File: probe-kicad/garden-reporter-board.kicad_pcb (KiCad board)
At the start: 2 copper layers, 21 parts, among them J1 70543-0106, J2 Conn_01x02, J3 70543-0002, J4 70543-0002, J5 70543-0002, Q1 TN0702N3-G, U1 MCP1700-3302E_TO92, U2 MCP1700-3302E_TO92

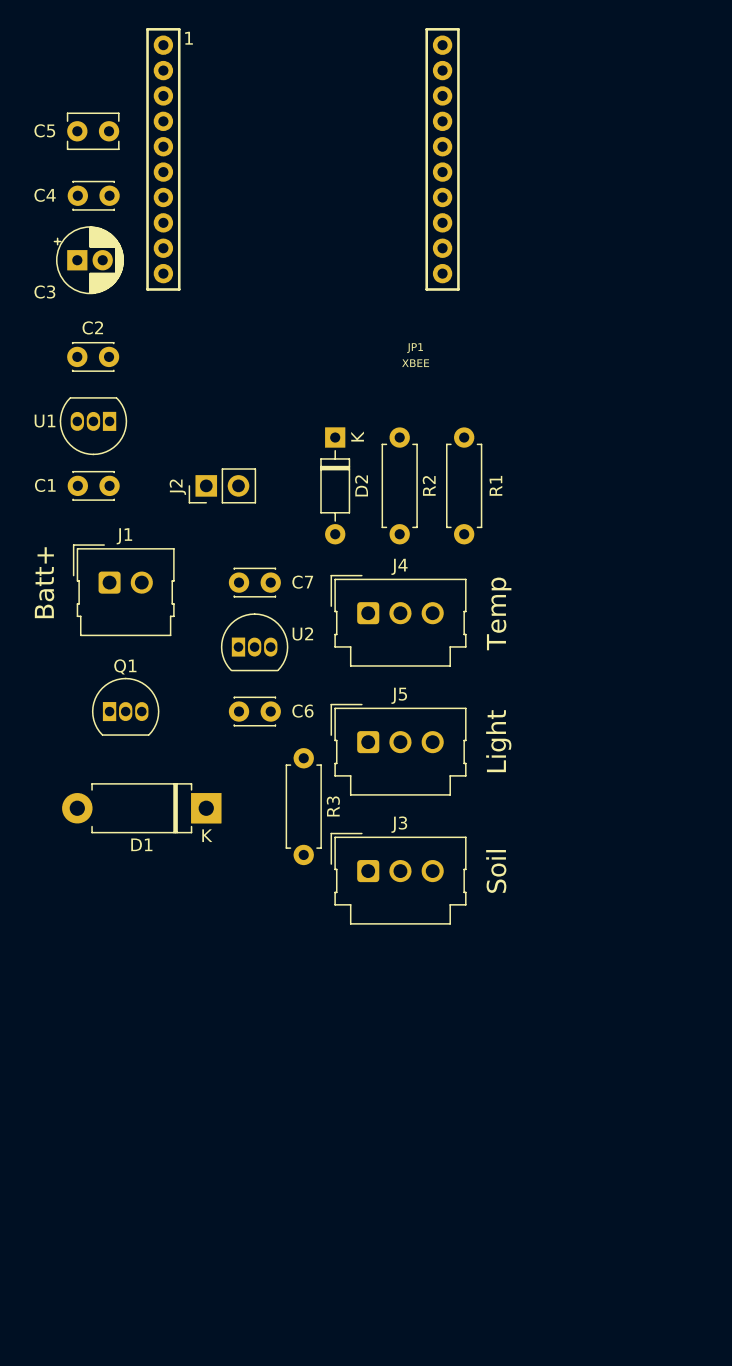
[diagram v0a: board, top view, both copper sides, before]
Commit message: Feature/probe pcb edge and routing
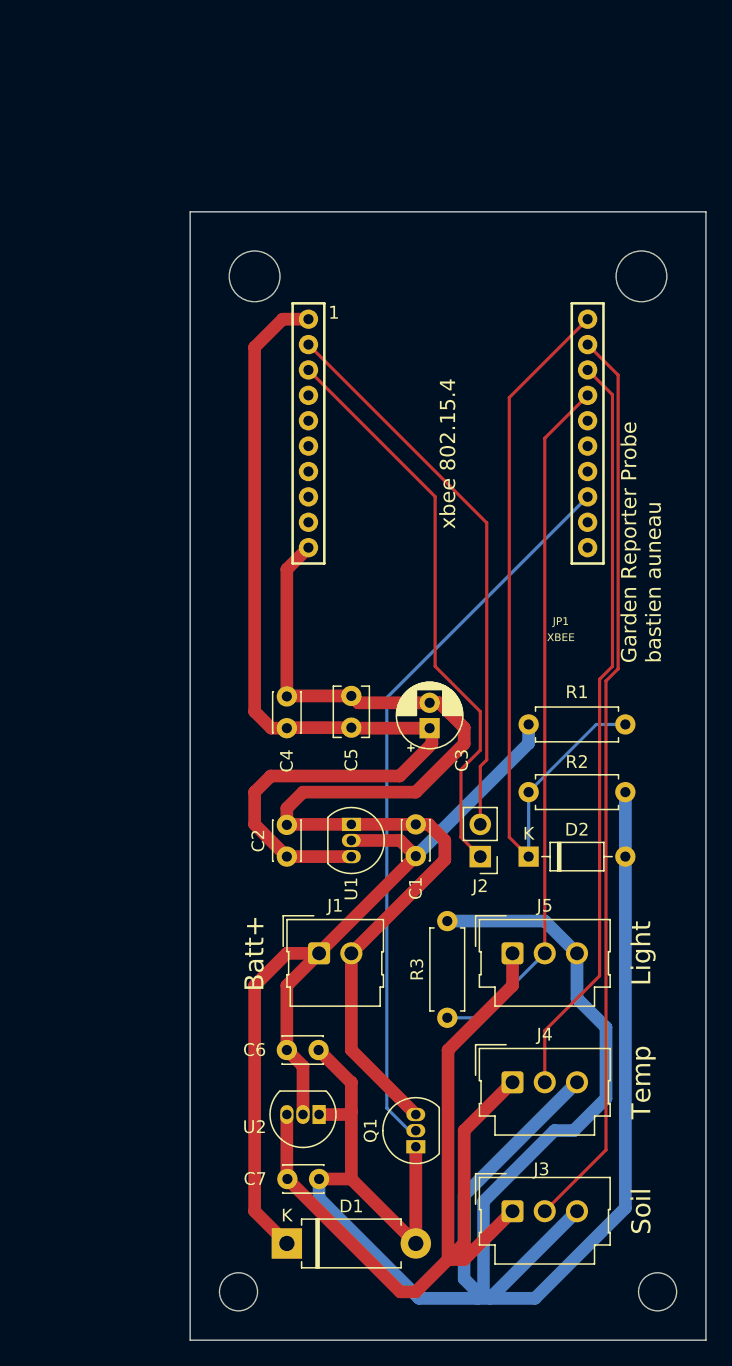
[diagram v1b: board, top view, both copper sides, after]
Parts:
- moved C5 51.7 mm to (146.1, 95.2), turned to 90 degrees
- moved C7 47.0 mm to (141.0, 130.8), turned to 0 degrees
- moved C3 46.2 mm to (152.2, 95.3), turned to 90 degrees
- moved C4 45.1 mm to (141.0, 95.3), turned to 90 degrees
- moved C2 42.7 mm to (141.0, 105.4), turned to 90 degrees
- moved Q1 41.9 mm to (151.1, 128.3), turned to 90 degrees
- moved C1 39.5 mm to (151.1, 105.4), turned to 90 degrees
- moved J4 38.7 mm to (158.8, 123.2)
- moved U2 37.4 mm to (143.5, 125.7), turned to 180 degrees
- moved U1 37.0 mm to (146.1, 102.9), turned to -90 degrees
- moved D2 36.4 mm to (160.0, 105.4), turned to 0 degrees
- moved J2 36.3 mm to (156.2, 105.4), turned to 180 degrees
- moved D1 34.9 mm to (141.0, 135.9), turned to 0 degrees
- moved J1 33.6 mm to (143.5, 113.0)
- moved R2 29.7 mm to (160.0, 100.3), turned to 0 degrees
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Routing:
- net GND1: track 0.00 -> 171.2 mm
- net -BATT: track 0.00 -> 85.8 mm
- net +3.3V: track 0.00 -> 76.3 mm
- net +BATT: track 0.00 -> 72.2 mm
- net /sensor_soil: track 0.00 -> 71.7 mm
- net +3.3VADC: track 0.00 -> 71.5 mm
- net /sensor_batt: track 0.00 -> 60.4 mm
- net /sensor_temp: track 0.00 -> 59.1 mm
- net /xbee_ON: track 0.00 -> 57.7 mm
- net /sensor_light: track 0.00 -> 55.1 mm
- net Net-(J2-Pad1): track 0.00 -> 45.2 mm
- net Net-(J2-Pad2): track 0.00 -> 43.8 mm
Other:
- board outline added: 40.6 x 88.9 mm
- board text added: "Garden Reporter Probe bastien auneau"
- board text added: "xbee 802.15.4"
